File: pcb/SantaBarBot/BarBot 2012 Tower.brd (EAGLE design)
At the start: 76.2 x 76.2 mm, 52 parts, among them J2 POWER_JACKSLT, U1 ATMEGA328P, U2 SN75HVD179D, U3 742G04DBVR, U4 LMV324IDR, U5 L298, Y1 16MHz

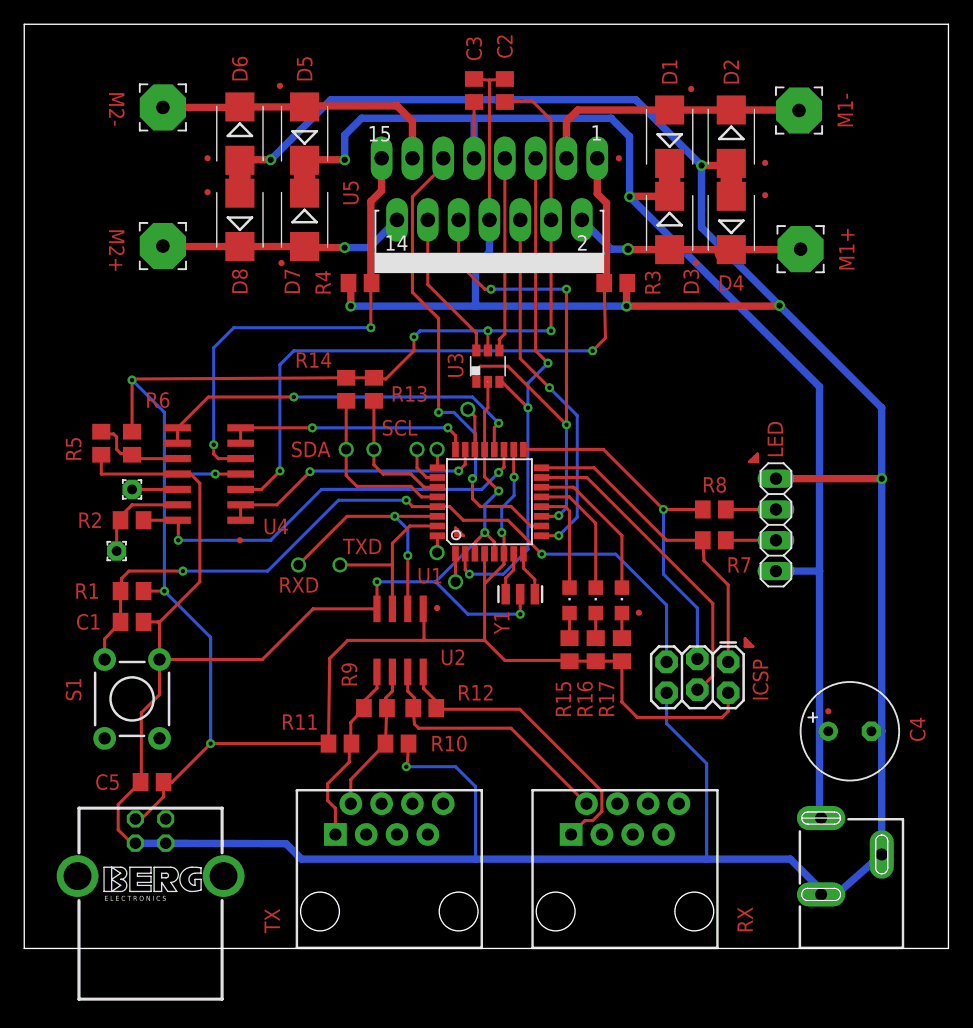
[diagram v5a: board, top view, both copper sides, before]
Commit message: Finalizing PCB.  Added DC over ethernet capability, added micro-usb connector footprint, changed power jack to more standard one.  Added mounting holes.  Cleaned up some traces.  Added new renders (top and bottom)
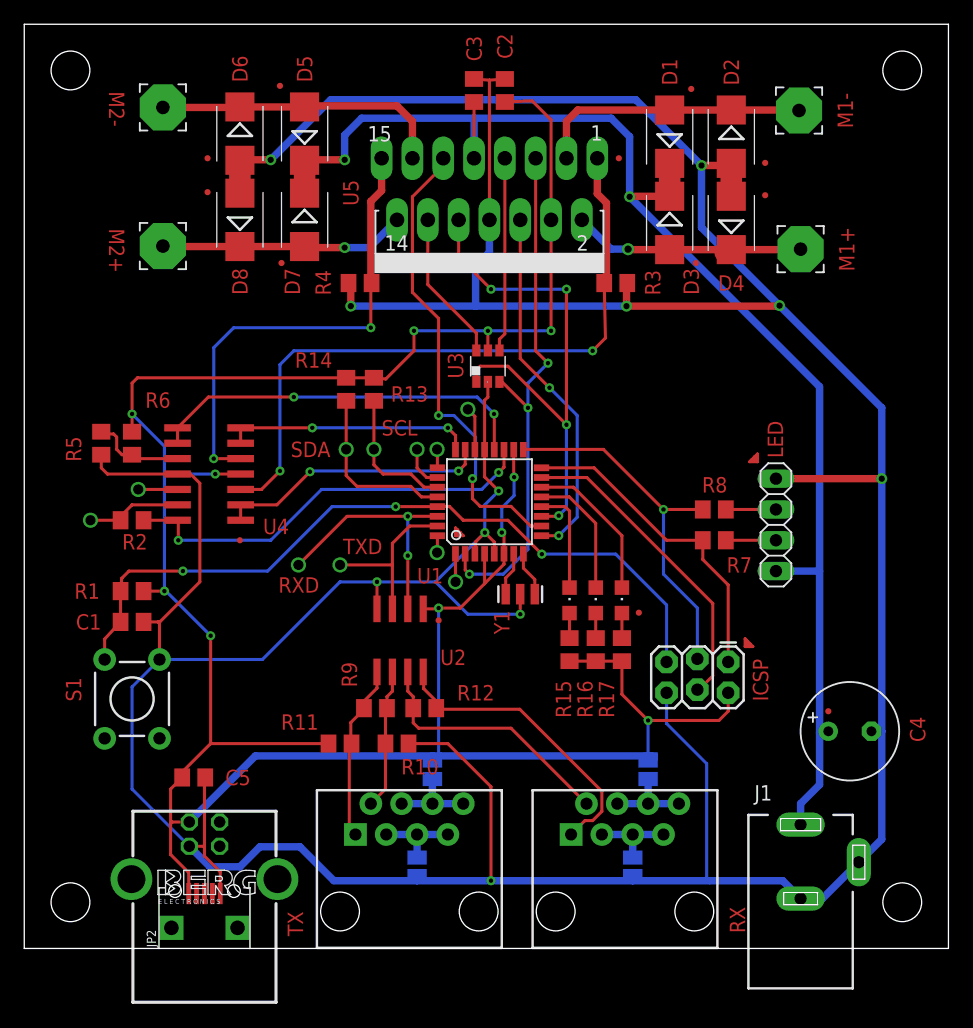
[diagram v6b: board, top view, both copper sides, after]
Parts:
- removed J2: POWER_JACKSLT, SparkFun-Connectors:POWER_JACK_SLOT
- removed PAD1, PAD2: (no value), wirepad:1,6/0,8
- added J1: DCJ0202, con-jack:DCJ0202
- added JP2: USB-RECEPTABLE, daspilker:FCI-10103594-0001LF
- added SJ1, SJ2, SJ3, SJ4: (no value), jumper:SJ
- moved JP1 4.45 mm to (14.9, 5.71)
- moved C5 3.45 mm to (14.0, 14.1), turned to 180 degrees
- moved TX 1.65 mm to (31.8, 3.05)
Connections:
- removed net N$3: PAD2.1, R2.2, U4.13
- removed net RJ_RX_3: RX.3
- removed net RJ_RX_4: RX.4
- removed net RJ_RX_5: RX.5
- removed net RJ_RX_6: RX.6
- removed net RJ_RX_7: RX.7
- removed net RJ_RX_8: RX.8
- removed net RJ_TX_3: TX.3
- removed net RJ_TX_4: TX.4
- removed net RJ_TX_5: TX.5
- removed net RJ_TX_6: TX.6
- removed net RJ_TX_7: TX.7
- removed net RJ_TX_8: TX.8
- removed net TP1: PAD1.1, U4.12
- new net RJ_RX_1: RX.3, RX.5, RX.7, SJ2.1
- new net RJ_RX_2: RX.4, RX.6, RX.8, SJ4.1
- new net RJ_TX_1: SJ1.1, TX.3, TX.5, TX.7
- new net RJ_TX_2: SJ3.1, TX.4, TX.6, TX.8
- new net U4D+: U4.12
- new net U4D-: R2.2, U4.13
- net +5V: now also JP2.1, SJ3.2, SJ4.2
- net +5V/2: now also J1.1; no longer J2.PWR
- net GND: now also J1.2, J1.3, JP2.5, SJ1.2, SJ2.2; no longer J2.GND@1, J2.GND@2
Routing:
- net +5V: track 193.7 -> 224.7 mm, vias 9 -> 11
- net GND: track 382.7 -> 396.3 mm
- net N$3: track 8.03 -> 0.00 mm
- net U4D-: track 0.00 -> 7.86 mm, vias 0 -> 1
- net RJ_TX_2: track 0.00 -> 7.11 mm
- net RJ_RX_2: track 0.00 -> 7.11 mm
- net RJ_TX_1: track 0.00 -> 6.98 mm
- net RJ_RX_1: track 0.00 -> 6.98 mm
- net TP1: track 3.75 -> 0.00 mm
- net U4D+: track 0.00 -> 3.24 mm, vias 0 -> 1
- net +5V/2: track 113.9 -> 115.1 mm
- net RS485_TX: track 15.6 -> 14.9 mm
- net !RS485_TX: track 12.6 -> 12.0 mm
